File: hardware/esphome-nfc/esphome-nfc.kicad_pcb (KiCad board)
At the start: 4 copper layers, 68.2 x 41 mm, 51 parts, among them SW1 TS-1187A-B-A-B, U1 ESP32-C3-WROOM-02, U2 PN7160A1HN/C100Y, U3 AP2112K-3.3TRG1, U4 USBLC6-2P6, Y1 Crystal_GND24

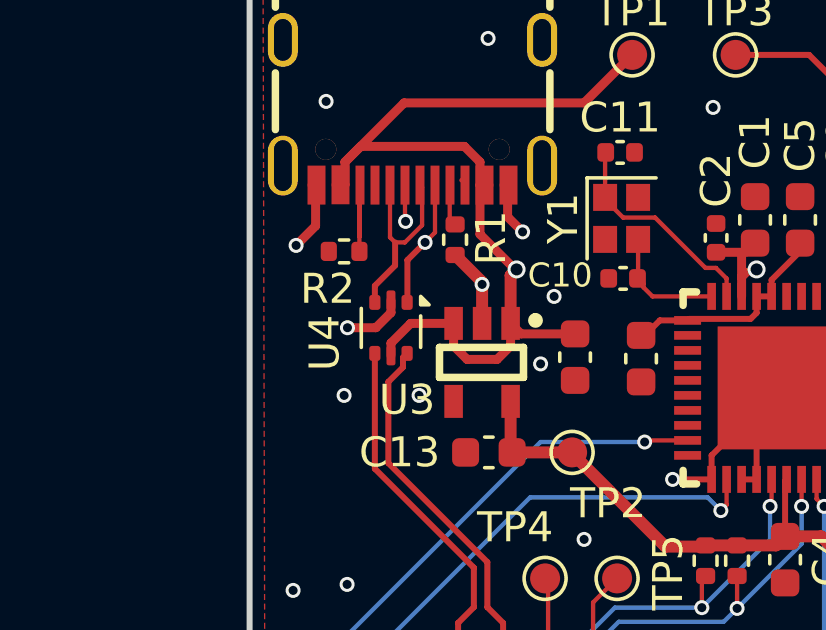
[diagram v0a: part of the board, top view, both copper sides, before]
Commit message: Use easyeda blueprint for USBLC6-2P6 to fix the rotation
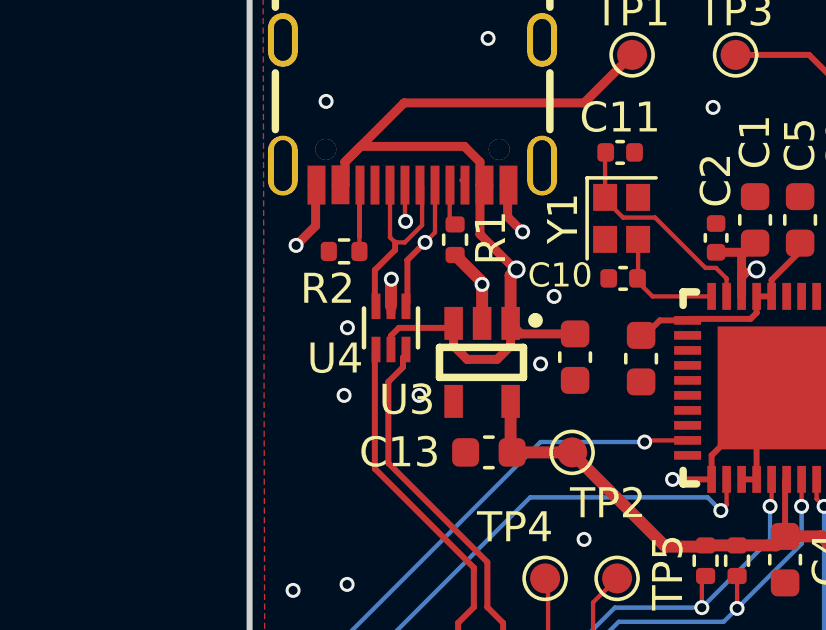
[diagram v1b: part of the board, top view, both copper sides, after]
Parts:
- U4: footprint Package_TO_SOT_SMD:SOT-666 -> easyeda2kicad:SOT-666-6_L1.6-W1.2-P0.50-LS1.6-BR
- turned U4 to 90 degrees
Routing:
- net GND: track 22.8 -> 22.0 mm, vias 35 -> 36
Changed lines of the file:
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@@
 		)
 	)
-	(footprint "Package_TO_SOT_SMD:SOT-666"
+	(footprint "easyeda2kicad:SOT-666-6_L1.6-W1.2-P0.50-LS1.6-BR"
 		(layer "F.Cu")
-		(at 160.9625 85.35 -90)
-		(descr "SOT666")
-		(tags "SOT-666")
+		(at 160.9625 85.35 90)
 		(property "Reference" "U4"
-			(at 0.5 2.2125 90)
+			(at -1.025 -1.8625 180)
 			(layer "F.SilkS")
 			(effects
@@
 		)
 		(property "Value" "USBLC6-2P6"
-			(at 0 1.75 90)
+			(at 0 4.5 90)
 			(layer "F.Fab")
 			(effects
@@
 			)
 		)
-		(property "Footprint" "Package_TO_SOT_SMD:SOT-666"
-			(at 0 0 -90)
-			(unlocked yes)
+		(property "Footprint" "easyeda2kicad:SOT-666-6_L1.6-W1.2-P0.50-LS1.6-BR"
+			(at 0 0 90)
 			(layer "F.Fab")
 			(hide yes)
@@
 		)
 		(property "Datasheet" "https://www.st.com/resource/en/datasheet/usblc6-2.pdf"
-			(at 0 0 -90)
-			(unlocked yes)
+			(at 0 0 90)
 			(layer "F.Fab")
 			(hide yes)
@@
 		)
 		(property "Description" "Very low capacitance ESD protection diode, 2 data-line, SOT-666"
-			(at 0 0 -90)
-			(unlocked yes)
+			(at 0 0 90)
 			(layer "F.Fab")
 			(hide yes)
@@
 		)
 		(property "LCSC" "C15999"
-			(at 0 0 -90)
+			(at 0 0 90)
 			(unlocked yes)
 			(layer "F.Fab")
@@
 		(attr smd)
 		(fp_line
-			(start 0.65 0.99)
-			(end -0.65 0.99)
+			(start 0.65 -0.9)
+			(end -0.65 -0.9)
 			(stroke
-				(width 0.12)
+				(width 0.15)
 				(type solid)
 			)
@@
 		)
 		(fp_line
-			(start 0.65 -0.99)
-			(end -0.4 -0.99)
+			(start 0.65 0.9)
+			(end -0.65 0.9)
 			(stroke
-				(width 0.12)
+				(width 0.15)
 				(type solid)
 			)
 			(layer "F.SilkS")
 		)
-		(fp_poly
-			(pts
-				(xy -0.77 -0.99) (xy -1.05 -0.99) (xy -0.77 -1.27) (xy -0.77 -0.99)
-			)
+		(fp_arc
+			(start 1.06 0.99)
+			(mid 1.06 0.99)
+			(end 1.06 0.99)
 			(stroke
-				(width 0.12)
+				(width 0.2)
 				(type solid)
 			)
-			(fill solid)
 			(layer "F.SilkS")
 		)
-		(fp_line
-			(start -1.5 1.1)
-			(end 1.5 1.1)
-			(stroke
-				(width 0.05)
-				(type solid)
-			)
-			(layer "F.CrtYd")
-		)
-		(fp_line
-			(start 1.5 1.1)
-			(end 1.5 -1.1)
-			(stroke
-				(width 0.05)
-				(type solid)
-			)
-			(layer "F.CrtYd")
-		)
-		(fp_line
-			(start -1.5 -1.1)
-			(end -1.5 1.1)
-			(stroke
-				(width 0.05)
-				(type solid)
-			)
-			(layer "F.CrtYd")
-		)
-		(fp_line
-			(start -1.5 -1.1)
-			(end 1.5 -1.1)
-			(stroke
-				(width 0.05)
-				(type solid)
-			)
-			(layer "F.CrtYd")
-		)
-		(fp_line
-			(start 0.65 0.85)
-			(end -0.65 0.85)
-			(stroke
-				(width 0.1)
-				(type solid)
-			)
-			(layer "F.Fab")
-		)
-		(fp_line
-			(start -0.65 -0.53)
-			(end -0.65 0.85)
-			(stroke
-				(width 0.1)
-				(type solid)
-			)
-			(layer "F.Fab")
-		)
-		(fp_line
-			(start -0.65 -0.53)
-			(end -0.33 -0.85)
-			(stroke
-				(width 0.1)
-				(type solid)
-			)
-			(layer "F.Fab")
-		)
-		(fp_line
-			(start 0.65 -0.85)
-			(end 0.65 0.85)
-			(stroke
-				(width 0.1)
-				(type solid)
-			)
-			(layer "F.Fab")
-		)
-		(fp_line
-			(start 0.65 -0.85)
-			(end -0.33 -0.85)
+		(fp_circle
+			(center 1.06 0.51)
+			(end 1.16 0.51)
 			(stroke
-				(width 0.1)
+				(width 0.2)
 				(type solid)
 			)
-			(layer "F.Fab")
+			(fill none)
+			(layer "Cmts.User")
 		)
-		(fp_line
-			(start 0.65 -0.85)
-			(end -0.33 -0.85)
+		(fp_circle
+			(center 0.8 0.83)
+			(end 0.83 0.83)
 			(stroke
-				(width 0.1)
+				(width 0.06)
 				(type solid)
 			)
+			(fill none)
 			(layer "F.Fab")
 		)
 		(fp_text user "${REFERENCE}"
-			(at 0 0 0)
+			(at 0 0 90)
 			(layer "F.Fab")
 			(effects
 				(font
-					(size 0.5 0.5)
-					(thickness 0.075)
+					(size 1 1)
+					(thickness 0.15)
 				)
 			)
 		)
-		(pad "1" smd roundrect
-			(at -0.85 -0.5375 270)
-			(size 0.5 0.375)
+		(pad "1" smd rect
+			(at 0.72 0.5 180)
+			(size 0.3 0.85)
 			(layers "F.Cu" "F.Paste" "F.Mask")
-			(roundrect_rratio 0.25)
 			(net 46 "/DN")
 			(pinfunction "I/O1")
 			(pintype "passive")
 		)
-		(pad "2" smd roundrect
-			(at -0.925 0 270)
-			(size 0.65 0.3)
+		(pad "2" smd rect
+			(at 0.72 0 180)
+			(size 0.3 0.85)
 			(layers "F.Cu" "F.Paste" "F.Mask")
-			(roundrect_rratio 0.25)
 			(net 1 "GND")
 			(pinfunction "GND")
 			(pintype "passive")
 		)
-		(pad "3" smd roundrect
-			(at -0.85 0.5375 270)
-			(size 0.5 0.375)
+		(pad "3" smd rect
+			(at 0.72 -0.5 180)
+			(size 0.3 0.85)
 			(layers "F.Cu" "F.Paste" "F.Mask")
-			(roundrect_rratio 0.25)
 			(net 45 "/DP")
 			(pinfunction "I/O2")
 			(pintype "passive")
 		)
-		(pad "4" smd roundrect
-			(at 0.85 0.5375 270)
-			(size 0.5 0.375)
+		(pad "4" smd rect
+			(at -0.72 -0.5 180)
+			(size 0.3 0.85)
 			(layers "F.Cu" "F.Paste" "F.Mask")
-			(roundrect_rratio 0.25)
 			(net 9 "/D+")
 			(pinfunction "I/O2")
 			(pintype "passive")
 		)
-		(pad "5" smd roundrect
-			(at 0.925 0 270)
-			(size 0.65 0.3)
+		(pad "5" smd rect
+			(at -0.72 0 180)
+			(size 0.3 0.85)
 			(layers "F.Cu" "F.Paste" "F.Mask")
-			(roundrect_rratio 0.25)
 			(net 19 "+5V")
 			(pinfunction "VBUS")
 			(pintype "passive")
 		)
-		(pad "6" smd roundrect
-			(at 0.85 -0.5375 270)
-			(size 0.5 0.375)
+		(pad "6" smd rect
+			(at -0.72 0.5 180)
+			(size 0.3 0.85)
 			(layers "F.Cu" "F.Paste" "F.Mask")
-			(roundrect_rratio 0.25)
 			(net 10 "/D-")
 			(pinfunction "I/O1")
 			(pintype "passive")
 		)
-		(model "${KICAD8_3DMODEL_DIR}/Package_TO_SOT_SMD.3dshapes/SOT-666.wrl"
+		(model "Z:/Dev/Kicad/easyeda2kicad/easyeda2kicad.3dshapes/SOT-666-6P_L1.6-W1.2-H0.6-LS1.6-P0.50.wrl"
 			(offset
-				(xyz 0 0 0)
+				(xyz -0 0.03 -0)
 			)
 			(scale
@@
 			)
 			(rotate
-				(xyz 0 0 0)
+				(xyz 0 0 180)
 			)
 		)
@@
 	)
 	(segment
-		(start 160.9625 84.842656)
-		(end 160.461156 85.344)
-		(width 0.3)
+		(start 160.9625 84.63)
+		(end 160.9625 83.7375)
+		(width 0.4)
 		(layer "F.Cu")
 		(net 1)
@@
 	)
 	(segment
+		(start 160.9625 83.7375)
+		(end 160.975 83.725)
+		(width 0.4)
+		(layer "F.Cu")
+		(net 1)
+	)
+	(segment
 		(start 158.45 80.71)
 		(end 158.33 80.59)
@@
 	)
 	(segment
-		(start 160.461156 85.344)
-		(end 159.512 85.344)
-		(width 0.3)
-		(layer "F.Cu")
-		(net 1)
-	)
-	(segment
 		(start 164 85.2)
 		(end 164 83.9)
@@
 	)
 	(via
+		(at 160.975 83.725)
+		(size 0.5)
+		(drill 0.3)
+		(layers "F.Cu" "B.Cu")
+		(net 1)
+	)
+	(via
 		(at 180.2 96)
 		(size 0.5)
@@
 	)
 	(segment
+		(start 160.9625 85.6125)
+		(end 161.225 85.35)
+		(width 0.2)
+		(layer "F.Cu")
+		(net 19)
+	)
+	(segment
 		(start 176.95 88.6)
 		(end 176.95 89.1)
@@
 	)
 	(segment
-		(start 163.93 82.23)
-		(end 165.1 83.4)
-		(width 0.3)
+		(start 161.225 85.35)
+		(end 162.9 85.35)
+		(width 0.2)
 		(layer "F.Cu")
 		(net 19)
 	)
 	(segment
-		(start 160.9625 86.275)
-		(end 160.9625 85.857344)
+		(start 163.93 82.23)
+		(end 165.1 83.4)
 		(width 0.3)
 		(layer "F.Cu")
@@
 	)
 	(segment
-		(start 161.619844 85.2)
+		(start 162.9 85.35)
 		(end 163.05 85.2)
-		(width 0.3)
+		(width 0.2)
+		(layer "F.Cu")
+		(net 19)
+	)
+	(segment
+		(start 160.9625 86.275)
+		(end 160.9625 85.6125)
+		(width 0.2)
 		(layer "F.Cu")
 		(net 19)
@@
 	)
 	(segment
-		(start 160.9625 85.857344)
-		(end 161.619844 85.2)
-		(width 0.3)
-		(layer "F.Cu")
-		(net 19)
-	)
-	(segment
 		(start 172.795 82.83)
 		(end 173.1 82.525)
@@
 	)
 	(segment
-		(start 160.425 83.945)
-		(end 161.1 83.27)
-		(width 0.2)
+		(start 162 81.925)
+		(end 162 80.66)
+		(width 0.145)
 		(layer "F.Cu")
 		(net 45)
 	)
 	(segment
-		(start 161.1 83.27)
-		(end 161.1 82.5)
+		(start 160.425 83.425)
+		(end 161.1 82.75)
 		(width 0.2)
 		(layer "F.Cu")
@@
 	)
 	(segment
-		(start 162 81.925)
-		(end 162 80.66)
-		(width 0.145)
-		(layer "F.Cu")
-		(net 45)
-	)
-	(segment
 		(start 162 80.66)
 		(end 161.93 80.59)
@@
 	)
 	(segment
-		(start 160.425 84.5)
-		(end 160.425 83.945)
-		(width 0.2)
-		(layer "F.Cu")
-		(net 45)
-	)
-	(segment
 		(start 161.1 82.5)
 		(end 161.425 82.5)
@@
 	)
 	(segment
+		(start 161.1 82.75)
+		(end 161.1 82.5)
+		(width 0.2)
+		(layer "F.Cu")
+		(net 45)
+	)
+	(segment
 		(start 161.1 82.5)
 		(end 160.93 82.33)
@@
 		(layer "F.Cu")
 		(net 45)
+	)
+	(segment
+		(start 160.425 84.5)
+		(end 160.425 83.425)
+		(width 0.2)
+		(layer "F.Cu")
+		(net 45)
